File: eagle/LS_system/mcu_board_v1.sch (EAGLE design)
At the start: 23 parts, among them IC2 LT1763CS8-3.3, IC3 STM32F4XX_64, Q2 PFET, X1 USBSMD, X2 MURDOCK_STACK

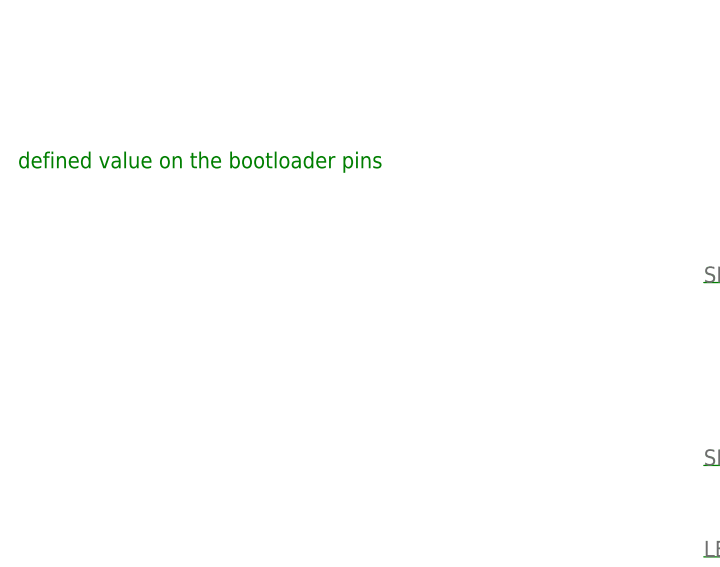
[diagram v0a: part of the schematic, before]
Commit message: conneced LEDs to switche 3v3
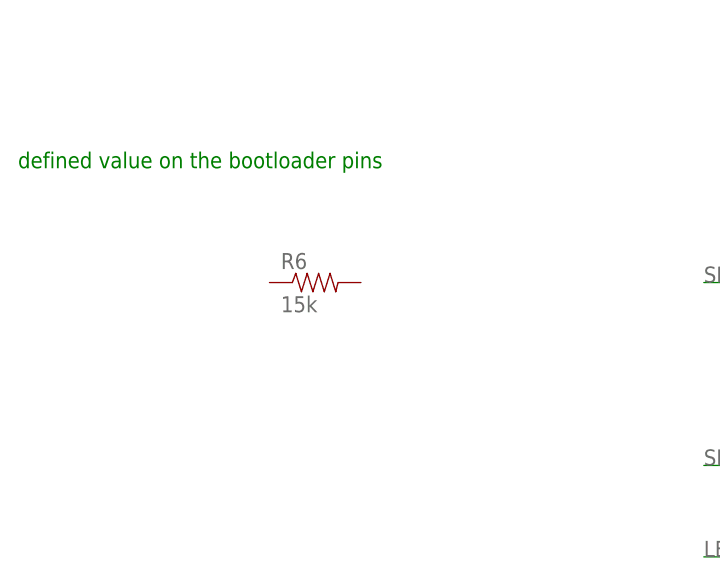
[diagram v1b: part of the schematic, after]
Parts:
- added R6: 15k, SparkFun-Resistors:RESISTOR0402-RES
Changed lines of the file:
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@@
 <?xml version="1.0" encoding="utf-8"?>
 <!DOCTYPE eagle SYSTEM "eagle.dtd">
-<eagle version="6.4">
+<eagle version="6.3">
 <drawing>
 <settings>
@@
 <part name="R5" library="SparkFun-Resistors" deviceset="RESISTOR" device="0402-RES" value="15k"/>
 <part name="GND3" library="SparkFun-Aesthetics" deviceset="GND" device=""/>
+<part name="R6" library="SparkFun-Resistors" deviceset="RESISTOR" device="0402-RES" value="15k"/>
 </parts>
 <sheets>
@@
 <instance part="R5" gate="G$1" x="-86.36" y="111.76" rot="R90"/>
 <instance part="GND3" gate="1" x="-86.36" y="104.14" smashed="yes"/>
+<instance part="R6" gate="G$1" x="-60.96" y="48.26"/>
 </instances>
 <busses>

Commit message: typo
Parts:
- removed R6: 15k, SparkFun-Resistors:RESISTOR0402-RES
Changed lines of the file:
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@@
 <part name="R5" library="SparkFun-Resistors" deviceset="RESISTOR" device="0402-RES" value="15k"/>
 <part name="GND3" library="SparkFun-Aesthetics" deviceset="GND" device=""/>
-<part name="R6" library="SparkFun-Resistors" deviceset="RESISTOR" device="0402-RES" value="15k"/>
 </parts>
 <sheets>
@@
 <instance part="R5" gate="G$1" x="-86.36" y="111.76" rot="R90"/>
 <instance part="GND3" gate="1" x="-86.36" y="104.14" smashed="yes"/>
-<instance part="R6" gate="G$1" x="-60.96" y="48.26"/>
 </instances>
 <busses>
